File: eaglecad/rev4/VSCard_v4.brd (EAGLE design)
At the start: 156.2 x 92.9 mm, 74 parts, among them IC1 74LS244N, IC2 16C550, IC3 CY62256LL-PC, IC4 74LS244N, IC5 74LS244N, IC6 74LS00N, IC7 74LS00N, IC8 74LS244N, J1 SERIAL-TTL, J2 RCA, J3 RCA, J4 RCA, J5 RCA, Q1 10.738635mhz, Q2 2N2222, U1 TMS4416, U11 SN76489, U2 TMS9118, U3 TMS4416, U4 SN76489, Y1 1.8432mhz

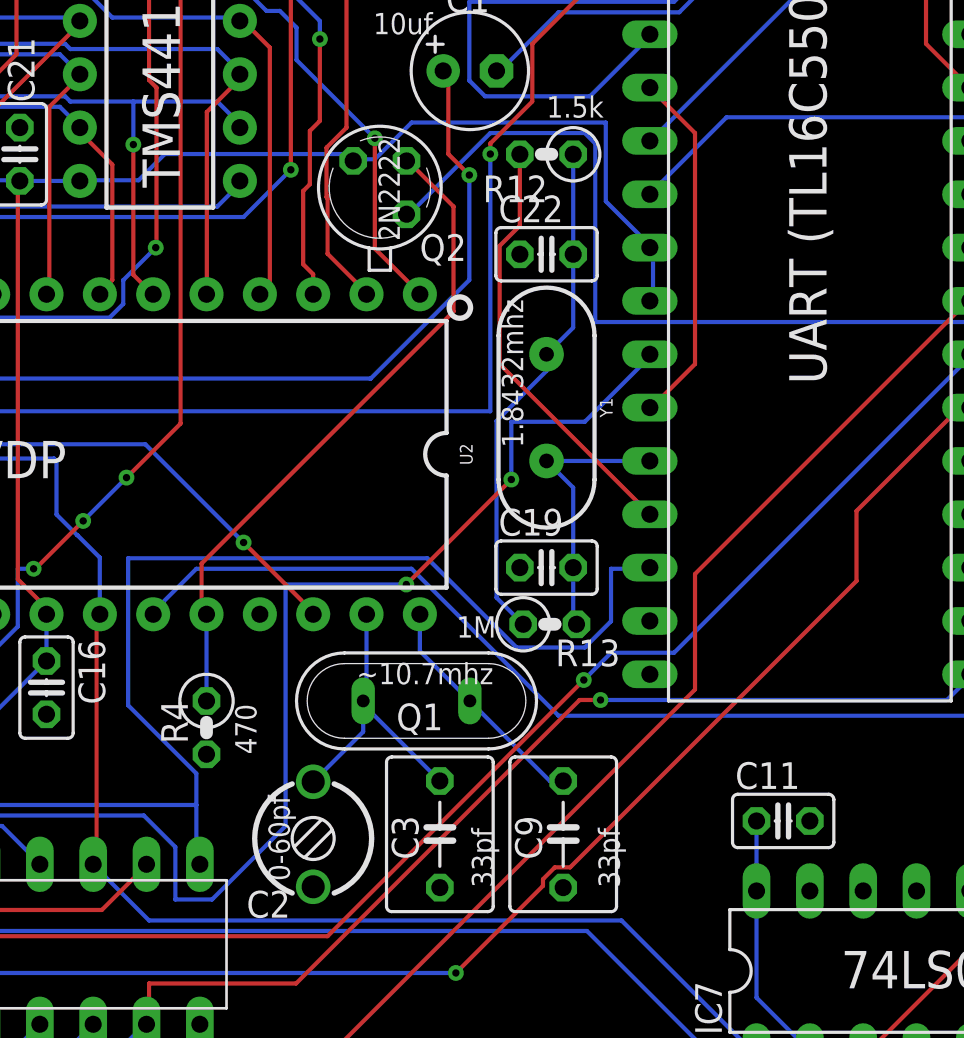
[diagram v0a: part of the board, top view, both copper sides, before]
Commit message: got rid of extra crystal for UART -- used VDP CPUCLK output instead
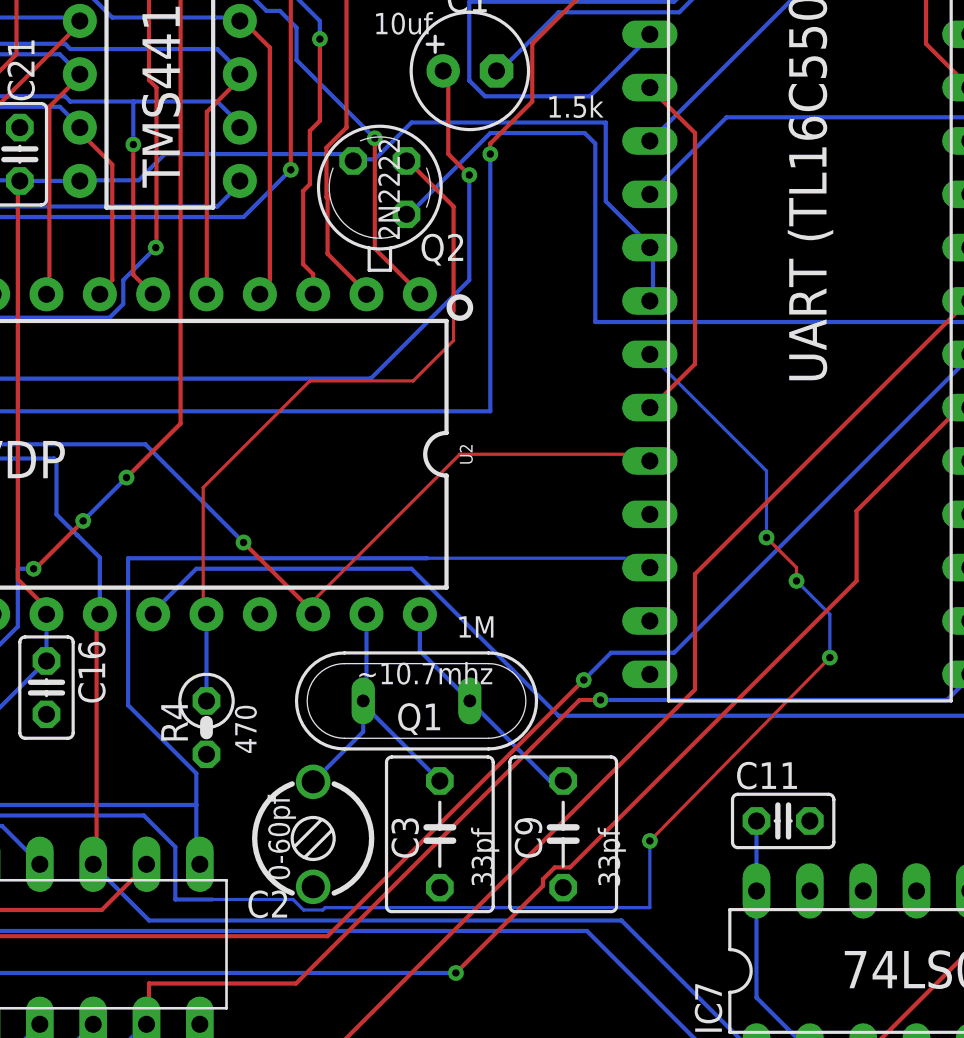
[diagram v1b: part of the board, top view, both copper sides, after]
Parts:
- removed C19: 20pf, rcl:C025-025X050
- removed C22: 30pf, rcl:C025-025X050
- removed R12: 1.5k, resistor:0207/2V
- removed R13: 1M, resistor:0207/2V
- removed Y1: 1.8432mhz, SparkFun-Clocks:HC49US
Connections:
- removed net N$12: IC2.17, R12.2
- removed net N$13: C22.2, R12.1, R13.1, Y1.1
- removed net N$19: C19.2, IC2.16, R13.2, Y1.2
- net GND: no longer C19.1, C22.1
- net SN76489-CLOCK: now also IC2.16
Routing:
- net N$13: track 24.4 -> 0.00 mm
- net N$12: track 20.5 -> 0.00 mm
- net SN76489-CLOCK: track 85.7 -> 105.4 mm
- net N$6: track 71.4 -> 86.0 mm, vias 2 -> 4
- net N$19: track 13.3 -> 0.00 mm
- net OUT*: track 161.9 -> 157.4 mm
- net COMVID: track 31.8 -> 34.8 mm
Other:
- board text removed: "1.8432mhz"
